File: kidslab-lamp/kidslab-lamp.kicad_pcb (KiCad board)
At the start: 2 copper layers, 87.7 x 130.4 mm, 43 parts, among them U1 Pico

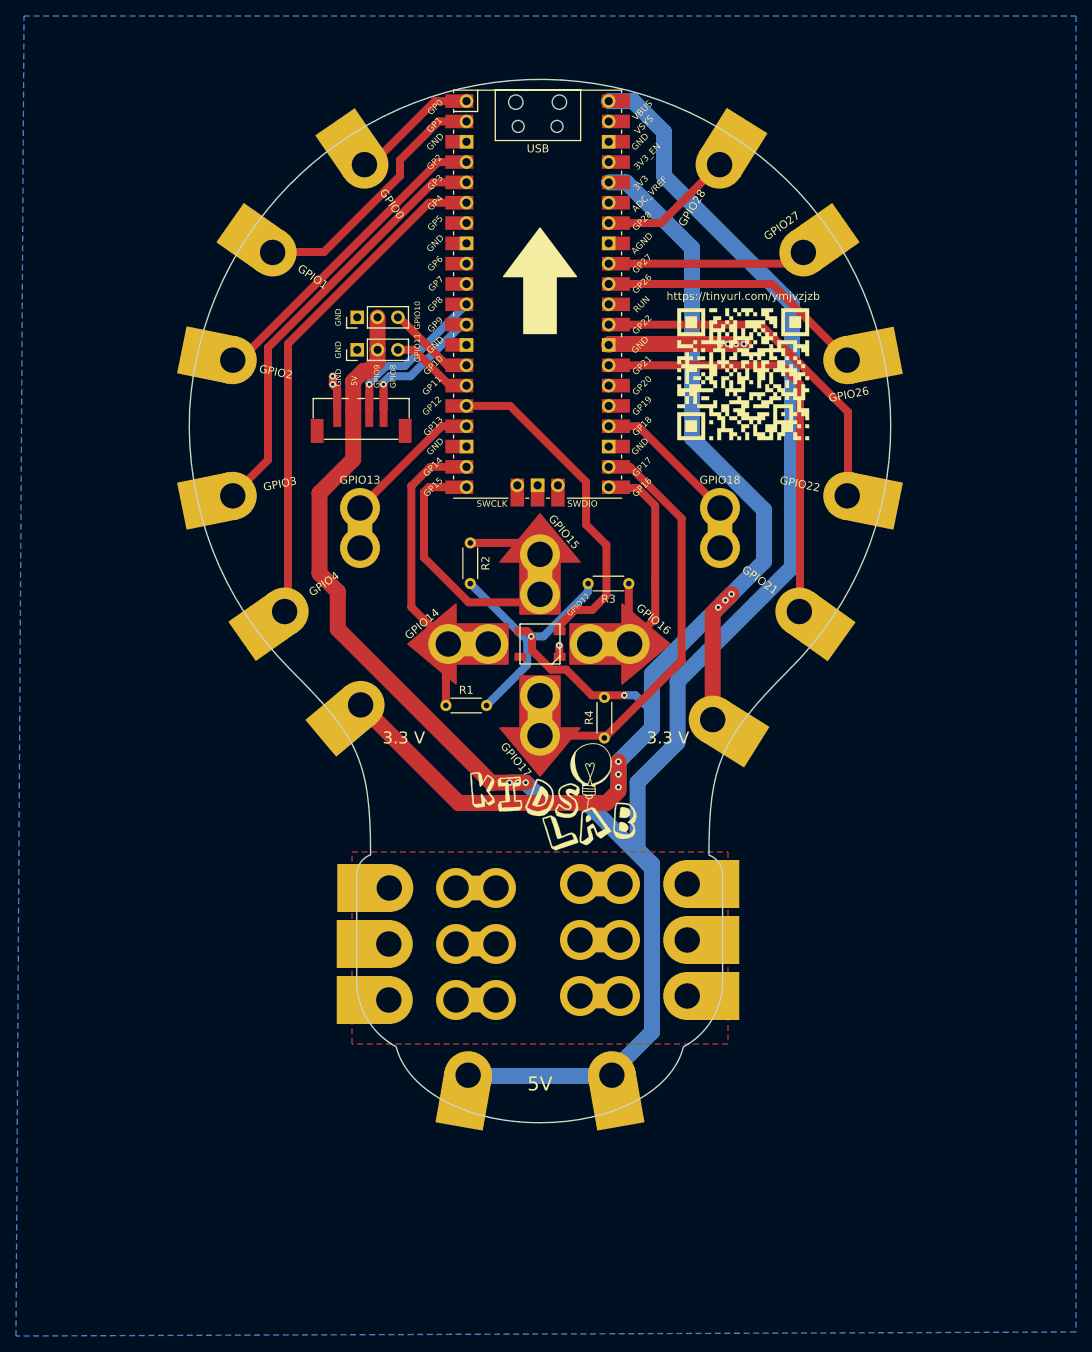
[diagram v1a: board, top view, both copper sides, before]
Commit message: adding layout
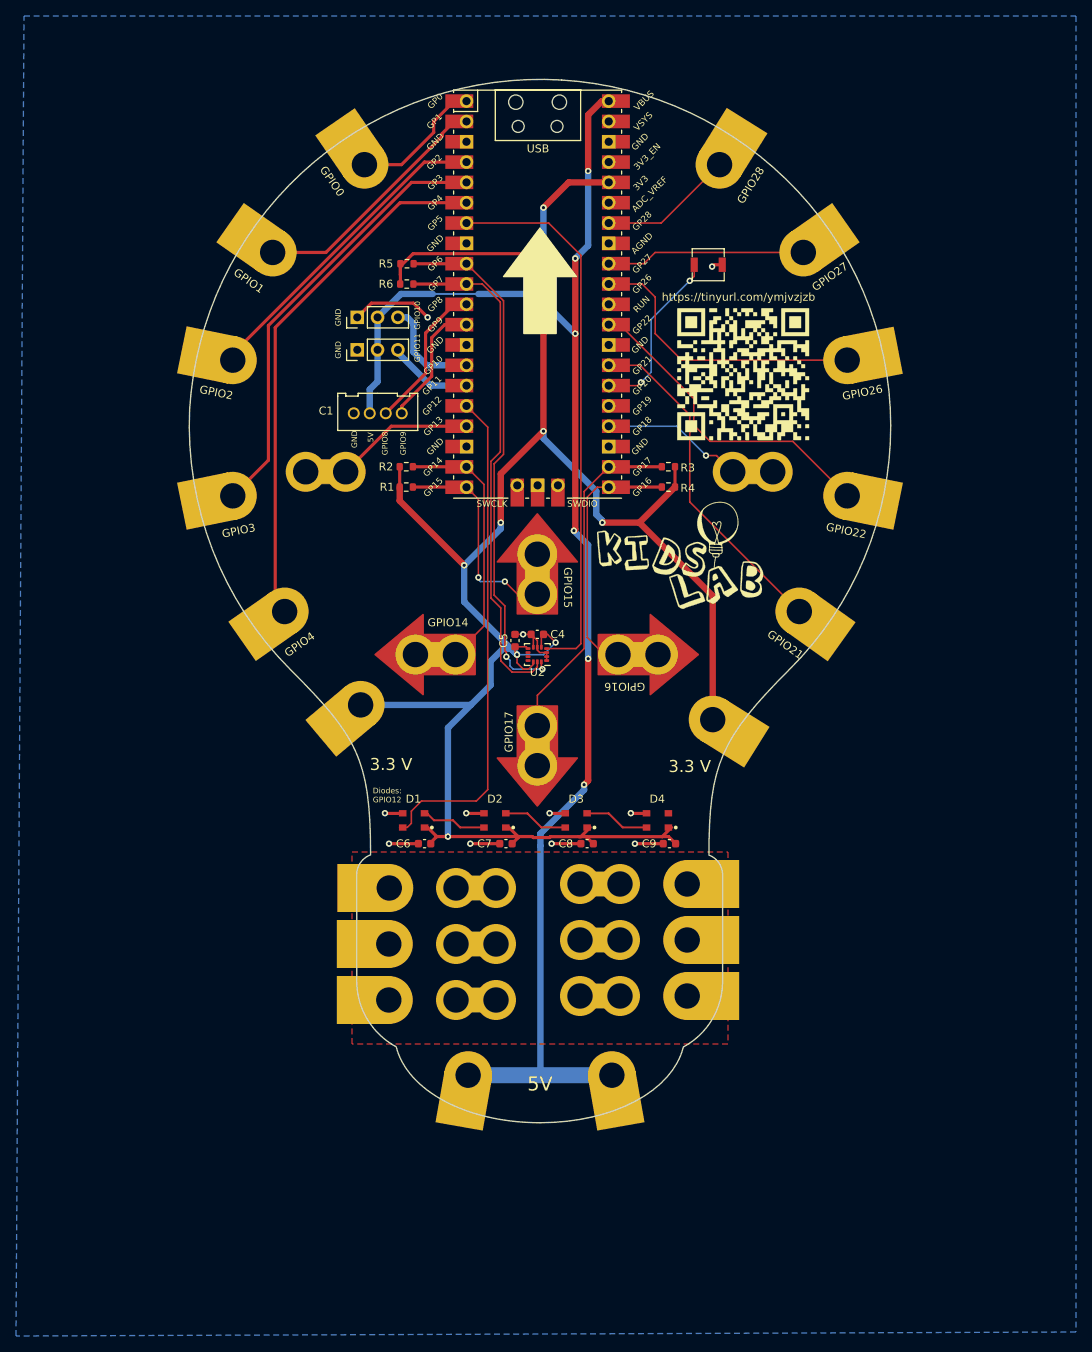
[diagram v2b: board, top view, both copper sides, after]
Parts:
- removed D12: SK6812, LED_SMD:LED_SK6812_PLCC4_5.0x5.0mm_P3.2mm
- added BZ1: Buzzer-FUET-4020, kidslab:Buzzer-FUET-4020, F.Cu at (171.0, 61.7)
- added C4: 100nF, Capacitor_SMD:C_0603_1608Metric, F.Cu at (149.6, 108.0)
- added C5: 100nF, Capacitor_SMD:C_0603_1608Metric, F.Cu at (146.8, 108.7)
- added C6: 100nF, Capacitor_SMD:C_0603_1608Metric, F.Cu at (135.5, 134.1)
- added C7: 100nF, Capacitor_SMD:C_0603_1608Metric, F.Cu at (145.7, 134.1)
- added C8: 100nF, Capacitor_SMD:C_0603_1608Metric, F.Cu at (155.8, 134.1)
- added C9: 100nF, Capacitor_SMD:C_0603_1608Metric, F.Cu at (166.1, 134.1)
- added D1: WS2812B-Mini, kidslab:WS2812B-Mini, F.Cu at (134.1, 131.2)
- added D2: WS2812B-Mini, kidslab:WS2812B-Mini, F.Cu at (144.3, 131.2)
- added D3: WS2812B-Mini, kidslab:WS2812B-Mini, F.Cu at (154.5, 131.2)
- added D4: WS2812B-Mini, kidslab:WS2812B-Mini, F.Cu at (164.6, 131.2)
- added R5: 10k, Resistor_SMD:R_0603_1608Metric, F.Cu at (133.3, 61.6)
- added R6: 10k, Resistor_SMD:R_0603_1608Metric, F.Cu at (133.3, 64.2)
- added U2: LSM6DS3, Package_LGA:LGA-14_3x2.5mm_P0.5mm_LayoutBorder3x4y, F.Cu at (149.6, 110.5)
- C1: value pin_header_1x3 -> HY-4A; footprint Connector_PinHeader_2.54mm:PinHeader_1x03_P2.54mm_Vertical -> kidslab:HY-4A-THT
- C2: value 114020163 -> pin_header_1x3; footprint kidslab:114020163 -> Connector_PinHeader_2.54mm:PinHeader_1x03_P2.54mm_Vertical
- R1, R2, R3, R4: value 10M -> 1M; footprint Resistor_THT:R_Axial_DIN0204_L3.6mm_D1.6mm_P5.08mm_Horizontal -> Resistor_SMD:R_0603_1608Metric
- moved R4 32.4 mm to (166.0, 89.5), turned to 0 degrees
- moved R1 27.8 mm to (133.2, 89.5), turned to 180 degrees
- moved R3 15.4 mm to (166.0, 87.0), turned to 0 degrees
- moved C2 12.7 mm to (127.1, 68.3), turned to 90 degrees
- moved R2 12.4 mm to (133.2, 87.0), turned to 180 degrees
- moved C1 12.3 mm to (129.7, 80.3), turned to 180 degrees
- moved GPIO13 8.23 mm to (123.2, 87.6), turned to 0 degrees
- moved GPIO18 8.13 mm to (176.5, 87.6), turned to 0 degrees
- moved GPIO14 4.32 mm to (136.8, 110.5)
- moved GPIO16 3.78 mm to (162.2, 110.5)
- moved GPIO17 3.76 mm to (149.6, 121.9)
- moved GPIO15 0.33 mm to (149.6, 100.4)
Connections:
- net 3.3V renamed +3V3
- C1 pad 1: GND -> GPIO9/GROVE_RX
- C1 pad 2: V_BUS -> GPIO8/GROVE_TX
- C1 pad 3: GPIO10 -> +5V
- C2 pad 1: grove_rx -> GND
- C2 pad 2: grove_tx -> +5V
- C2 pad 3: V_BUS -> GPIO10
- C3 pad 2: V_BUS -> +5V
- E37 pad 1: V_BUS -> +5V
- E38 pad 1: V_BUS -> +5V
- R1 pad 1: GPIO14 -> GPIO15
- R2 pad 1: GPIO15 -> GPIO14
- R3 pad 1: GPIO16 -> GPIO17
- R4 pad 1: GPIO17 -> GPIO16
- U1 pad 10: unconnected-(U1-Pad10) -> GPIO7/SCL1
- U1 pad 11: grove_tx -> GPIO8/GROVE_TX
- U1 pad 12: grove_rx -> GPIO9/GROVE_RX
- U1 pad 26: unconnected-(U1-Pad26) -> GPIO20/Buzzer
- U1 pad 40: V_BUS -> +5V
- U1 pad 7: unconnected-(U1-Pad7) -> GPIO5/INTR
- U1 pad 9: unconnected-(U1-Pad9) -> GPIO6/SDA1
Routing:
- net V_BUS: track 258.9 -> 0.00 mm, vias 3 -> 0
- net +5V: track 0.00 -> 185.6 mm, vias 0 -> 6
- net GPIO5/INTR: track 0.00 -> 69.1 mm
- net GPIO6/SDA1: track 0.00 -> 65.3 mm, vias 0 -> 2
- net GPIO7/SCL1: track 0.00 -> 63.7 mm
- net +3V3: track 205.1 -> 266.3 mm, vias 8 -> 9
- net GPIO20/Buzzer: track 0.00 -> 21.7 mm, vias 0 -> 2
- net GPIO12: track 42.3 -> 62.9 mm
- net grove_tx: track 19.5 -> 0.00 mm, vias 1 -> 0
- net GPIO8/GROVE_TX: track 0.00 -> 18.7 mm
- net GND: track 22.7 -> 41.4 mm, vias 7 -> 11
- net grove_rx: track 16.7 -> 0.00 mm, vias 1 -> 0
- net GPIO9/GROVE_RX: track 0.00 -> 16.0 mm
- net GPIO15: track 40.1 -> 27.0 mm, vias 0 -> 2
- net Net-(U1-GPIO21): track 53.4 -> 43.0 mm
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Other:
- board text added: "Diodes: GPIO12"
- board text removed: "GPIO12"

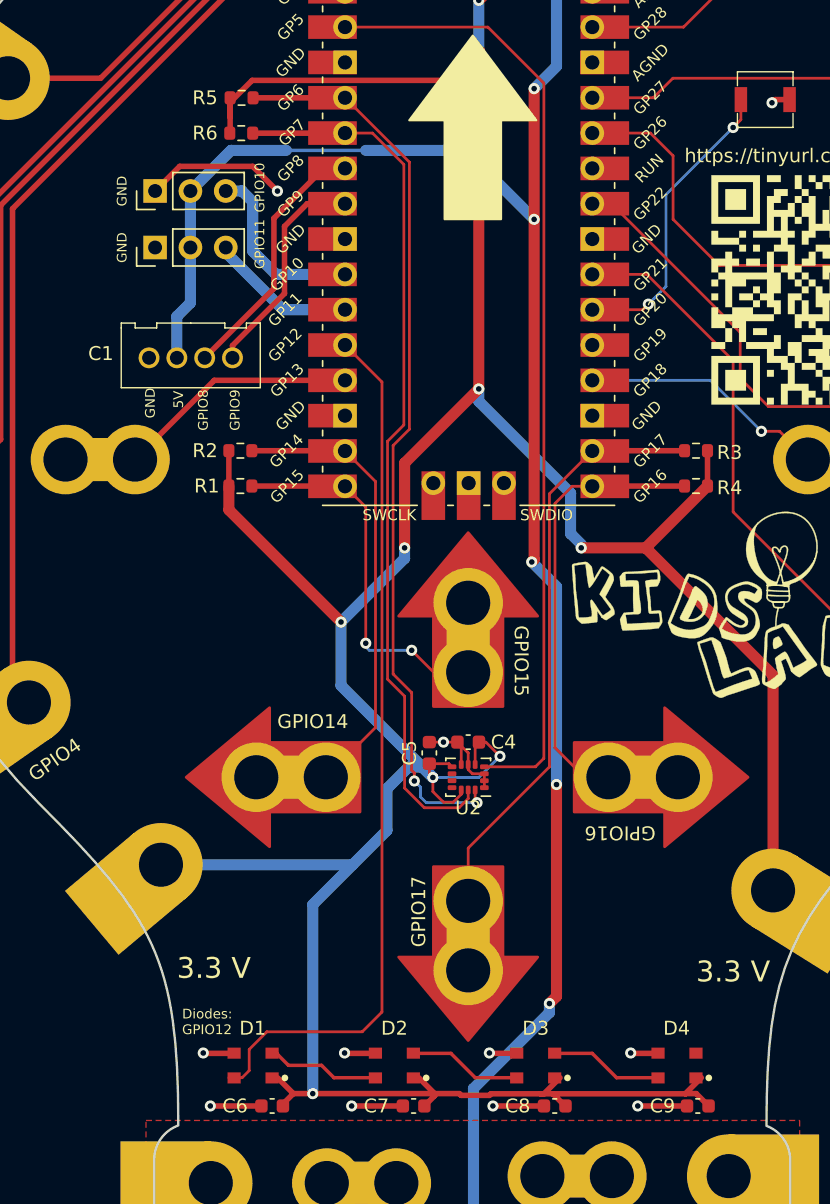
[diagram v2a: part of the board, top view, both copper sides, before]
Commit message: fixing some silkscreen issues
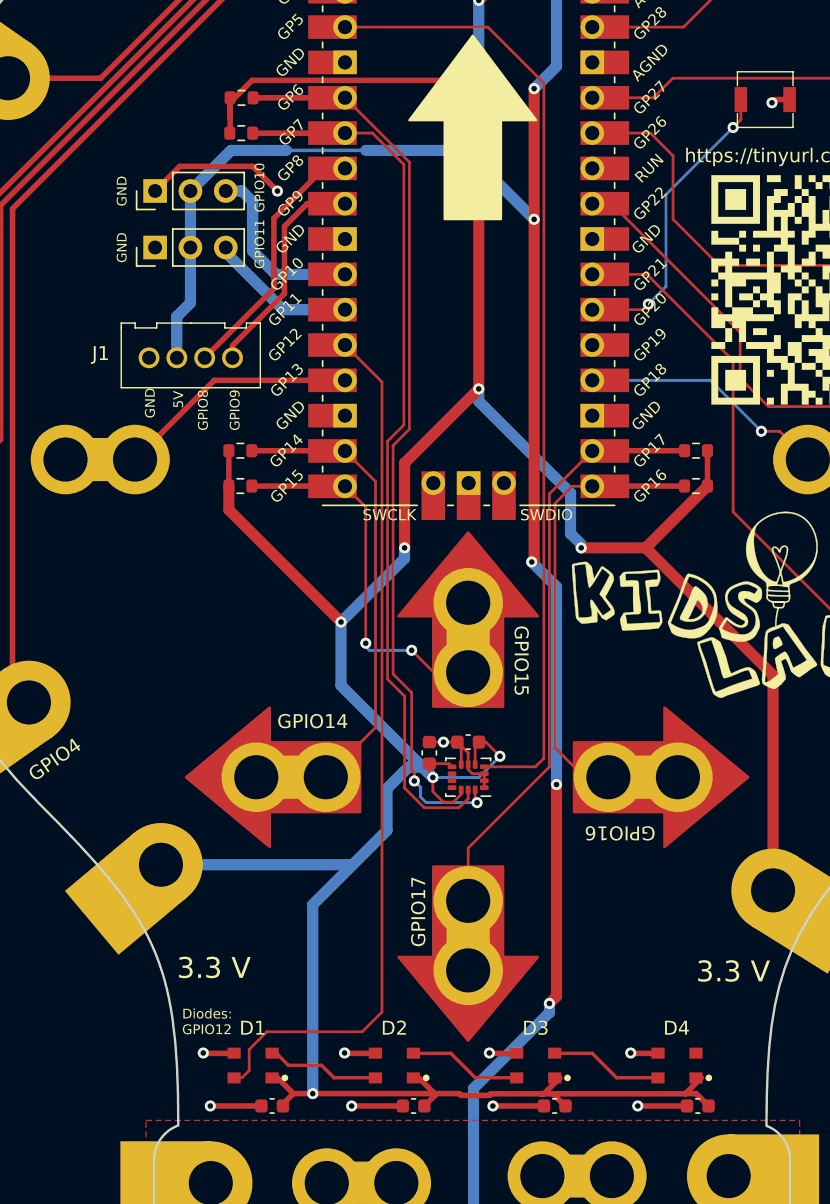
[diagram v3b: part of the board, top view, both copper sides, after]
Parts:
- renumbered C1 to J1, C2 to J2, C3 to J3
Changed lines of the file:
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@@
   (setup
     (stackup
-      (layer "F.SilkS" (type "Top Silk Screen"))
+      (layer "F.SilkS" (type "Top Silk Screen") (color "Black"))
       (layer "F.Paste" (type "Top Solder Paste"))
-      (layer "F.Mask" (type "Top Solder Mask") (thickness 0.01))
+      (layer "F.Mask" (type "Top Solder Mask") (color "White") (thickness 0.01))
       (layer "F.Cu" (type "copper") (thickness 0.035))
-      (layer "dielectric 1" (type "core") (thickness 1.51) (material "FR4") (epsilon_r 4.5) (loss_tangent 0.02))
+      (layer "dielectric 1" (type "core") (color "FR4 natural") (thickness 1.51) (material "FR4") (epsilon_r 4.5) (loss_tangent 0.02))
       (layer "B.Cu" (type "copper") (thickness 0.035))
-      (layer "B.Mask" (type "Bottom Solder Mask") (thickness 0.01))
+      (layer "B.Mask" (type "Bottom Solder Mask") (color "White") (thickness 0.01))
       (layer "B.Paste" (type "Bottom Solder Paste"))
-      (layer "B.SilkS" (type "Bottom Silk Screen"))
+      (layer "B.SilkS" (type "Bottom Silk Screen") (color "Black"))
       (copper_finish "None")
       (dielectric_constraints no)
@@
     (property "ki_keywords" "R res resistor")
     (attr smd)
-    (fp_text reference "R2" (at 2.54 0) (layer "F.SilkS")
+    (fp_text reference "R2" (at 2.54 0) (layer "F.SilkS") hide
         (effects (font (size 1 1) (thickness 0.15)))
     )
@@
     (property "ki_keywords" "R res resistor")
     (attr smd)
-    (fp_text reference "R6" (at -2.604 0) (layer "F.SilkS")
+    (fp_text reference "R6" (at -2.604 0) (layer "F.SilkS") hide
         (effects (font (size 1 1) (thickness 0.15)))
     )
@@
     (property "ki_keywords" "cap capacitor")
     (attr smd)
-    (fp_text reference "C7" (at 2.68 0) (layer "F.SilkS")
+    (fp_text reference "C7" (at 2.68 0) (layer "F.SilkS") hide
         (effects (font (size 1 1) (thickness 0.15)))
     )
@@
     (property "ki_keywords" "cap capacitor")
     (attr smd)
-    (fp_text reference "C4" (at -2.54 0) (layer "F.SilkS")
+    (fp_text reference "C4" (at -2.54 0) (layer "F.SilkS") hide
         (effects (font (size 1 1) (thickness 0.15)))
     )
@@
     (property "ki_keywords" "cap capacitor")
     (attr smd)
-    (fp_text reference "C9" (at 2.54 0) (layer "F.SilkS")
+    (fp_text reference "C9" (at 2.54 0) (layer "F.SilkS") hide
         (effects (font (size 1 1) (thickness 0.15)))
     )
@@
     (property "ki_keywords" "cap capacitor")
     (attr smd)
-    (fp_text reference "C6" (at 2.667 0) (layer "F.SilkS")
+    (fp_text reference "C6" (at 2.667 0) (layer "F.SilkS") hide
         (effects (font (size 1 1) (thickness 0.15)))
     )
@@
     (property "ki_keywords" "connector")
     (attr through_hole)
-    (fp_text reference "C1" (at 6.4676 0.3048 unlocked) (layer "F.SilkS")
+    (fp_text reference "J1" (at 6.4676 0.3048 unlocked) (layer "F.SilkS")
         (effects (font (size 1 1) (thickness 0.15)))
     )
@@
     (property "ki_keywords" "R res resistor")
     (attr smd)
-    (fp_text reference "R3" (at 2.413 0.127) (layer "F.SilkS")
+    (fp_text reference "R3" (at 2.413 0.127) (layer "F.SilkS") hide
         (effects (font (size 1 1) (thickness 0.15)))
     )
@@
     (property "ki_keywords" "Accelerometer Gyroscope MEMS")
     (attr smd)
-    (fp_text reference "U2" (at 0 -2.2) (layer "F.SilkS")
+    (fp_text reference "U2" (at 0 -2.2) (layer "F.SilkS") hide
         (effects (font (size 1 1) (thickness 0.15)))
     )
@@
     (property "ki_keywords" "R res resistor")
     (attr smd)
-    (fp_text reference "R1" (at 2.413 0) (layer "F.SilkS")
+    (fp_text reference "R1" (at 2.413 0) (layer "F.SilkS") hide
         (effects (font (size 1 1) (thickness 0.15)))
     )
@@
     (property "ki_keywords" "cap capacitor")
     (attr smd)
-    (fp_text reference "C5" (at 0 -1.43 90) (layer "F.SilkS")
+    (fp_text reference "C5" (at 0 -1.43 90) (layer "F.SilkS") hide
         (effects (font (size 1 1) (thickness 0.15)))
     )
@@
     (property "Sheetfile" "components-sheet.kicad_sch")
     (property "Sheetname" "Components")
-    (property "exclude_from_bom" "")
-    (attr through_hole exclude_from_pos_files exclude_from_bom)
-    (fp_text reference "C3" (at 0 -2.33 90) (layer "F.SilkS") hide
+    (attr through_hole exclude_from_pos_files)
+    (fp_text reference "J3" (at 0 -2.33 90) (layer "F.SilkS") hide
         (effects (font (size 1 1) (thickness 0.15)))
     )
@@
     (property "Sheetfile" "components-sheet.kicad_sch")
     (property "Sheetname" "Components")
-    (property "exclude_from_bom" "")
-    (attr through_hole exclude_from_pos_files exclude_from_bom)
-    (fp_text reference "C2" (at 0 -2.33 90) (layer "F.SilkS") hide
+    (attr through_hole exclude_from_pos_files)
+    (fp_text reference "J2" (at 0 -2.33 90) (layer "F.SilkS") hide
         (effects (font (size 1 1) (thickness 0.15)))
     )
@@
     (property "ki_keywords" "R res resistor")
     (attr smd)
-    (fp_text reference "R4" (at 2.413 0.127) (layer "F.SilkS")
+    (fp_text reference "R4" (at 2.413 0.127) (layer "F.SilkS") hide
         (effects (font (size 1 1) (thickness 0.15)))
     )
@@
     (property "ki_keywords" "R res resistor")
     (attr smd)
-    (fp_text reference "R5" (at -2.6294 0) (layer "F.SilkS")
+    (fp_text reference "R5" (at -2.6294 0) (layer "F.SilkS") hide
         (effects (font (size 1 1) (thickness 0.15)))
     )
@@
     (property "ki_keywords" "cap capacitor")
     (attr smd)
-    (fp_text reference "C8" (at 2.667 0) (layer "F.SilkS")
+    (fp_text reference "C8" (at 2.667 0) (layer "F.SilkS") hide
         (effects (font (size 1 1) (thickness 0.15)))
     )
